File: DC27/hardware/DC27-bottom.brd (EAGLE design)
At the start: 102.4 x 117.6 mm, 86 parts, among them IC2 LDL112D33R, IC3 FT2232HL-REEL, IC4 93LC46BT-I_OT, J1 DN PAIR, J2 JTAG, J3 Battery, U2 ESP-WROOM-32, Y1 ABM7-12.000MHZ-D2Y-T

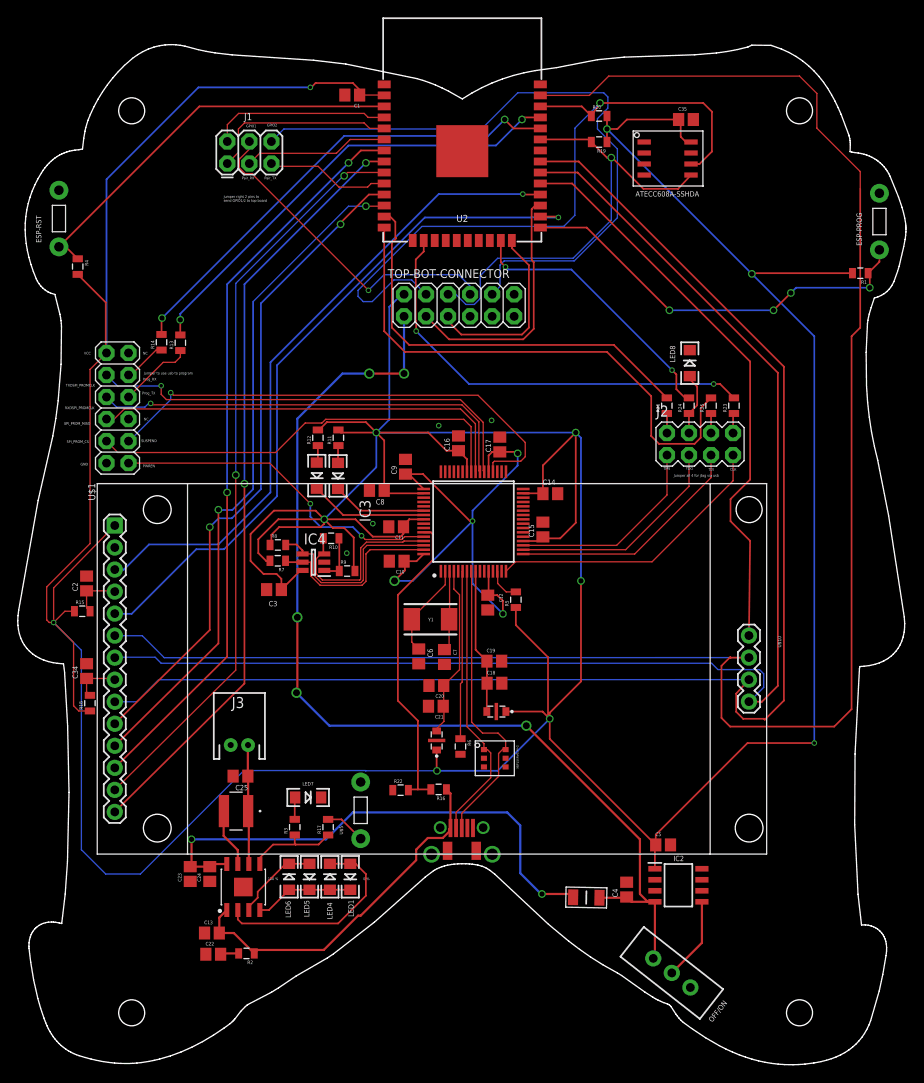
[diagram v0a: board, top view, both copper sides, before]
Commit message: Fixed copper ground planes
Fixed copper ground planes
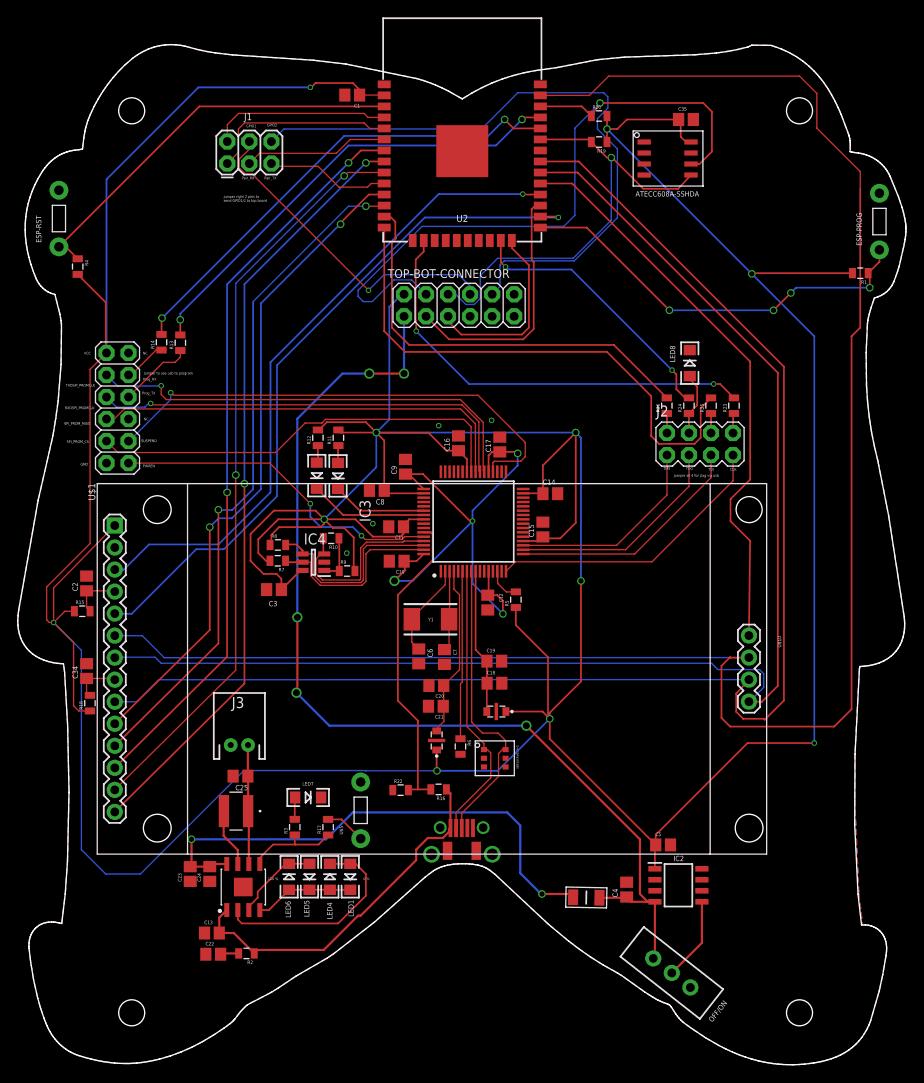
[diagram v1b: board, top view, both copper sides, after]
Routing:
- added copper zone on layer 1, net GND
- added copper zone on layer 16, net GND

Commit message: removed apa 102s from top board swapped led driver for atmega4089 put on programming pads bottom board adding paring headers on bottom board added 1206 56 OHM resistors to each LED top board pulled out UPDI pin on top board for programming the atmega chip
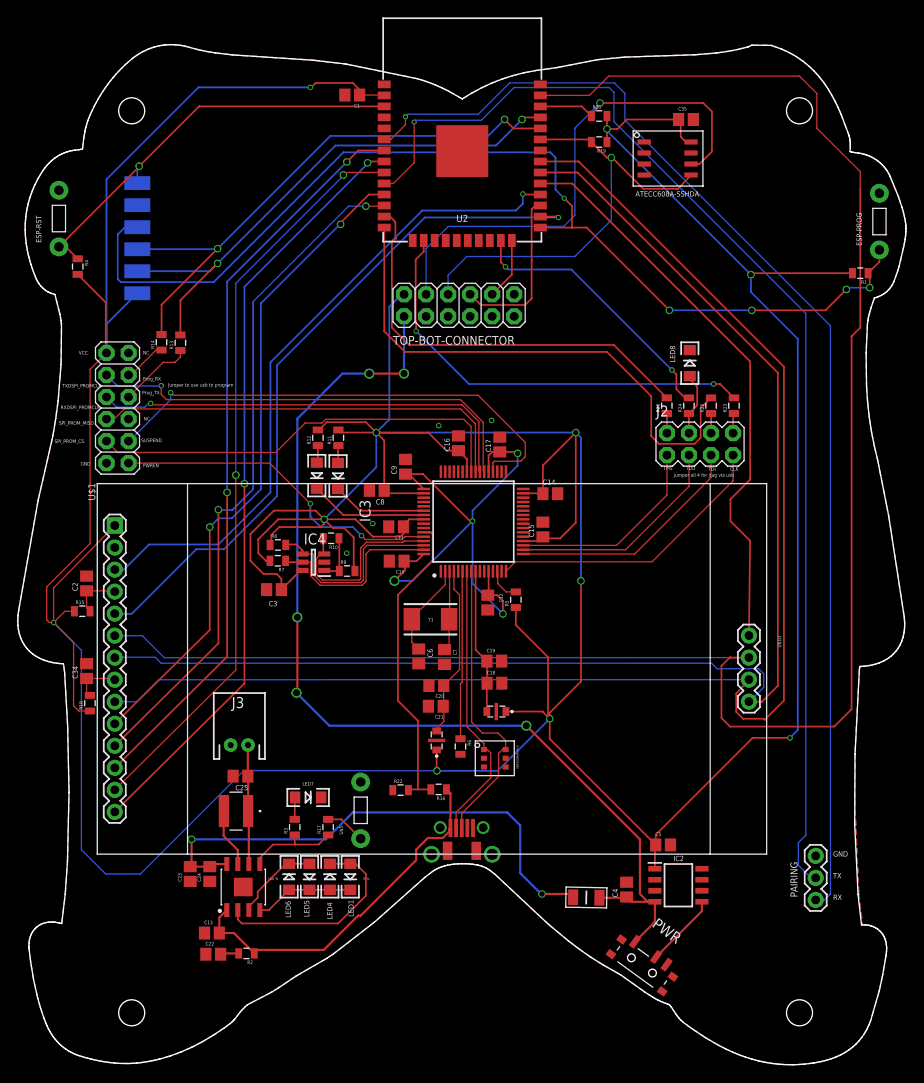
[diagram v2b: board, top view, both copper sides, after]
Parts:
- removed J1: DN PAIR, connector:2X3
- removed OFF/ON: Brd Power, switches:SWITCH-SPDT_KIT
- added J4: Program Port, connector:1X06-SMD-POGO
- added PWR: MSS3-V-T_R, switches:MSS3VTR
- added U$6: PAIRING, connector:1X03
- R3: value 10 R -> 1 K
- moved U$9 3.20 mm to (53.6, 108.0)
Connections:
- removed net N$2: IC2.5, OFF/ON.2
- removed net SAO-GPIO1: J1.4, TOP-BOT-CONNECTOR.8
- removed net SAO-GPIO2: J1.6, TOP-BOT-CONNECTOR.10
- new net EN: IC2.5, PWR.B1
- net APA102_CLK: now also TOP-BOT-CONNECTOR.10; no longer TOP-BOT-CONNECTOR.5
- net APA102_DATA: now also TOP-BOT-CONNECTOR.8; no longer TOP-BOT-CONNECTOR.3
- net ESP-EN: now also J4.1
- net ESP-IO0: now also J4.3
- net GND: now also J4.2, PWR.C1, U$6.3; no longer OFF/ON.1
- net PAIR_RX: now also U$6.1; no longer J1.3
- net PAIR_TX: now also U$6.2; no longer J1.5
- net PROG_RX: now also J4.4
- net PROG_TX: now also J4.5
- net SVN: no longer J1.1
- net SVP: no longer J1.2
- net VBAT: now also PWR.A1; no longer OFF/ON.3
- net VCC: now also J4.6
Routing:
- net PAIR_TX: track 14.3 -> 135.3 mm, vias 0 -> 1
- net PAIR_RX: track 16.7 -> 135.6 mm, vias 0 -> 1
- net SAO-GPIO2: track 76.2 -> 0.00 mm
- net ESP-IO0: track 48.0 -> 121.7 mm, vias 4 -> 5
- net SAO-GPIO1: track 38.2 -> 0.00 mm, vias 1 -> 0
- net SVN: track 21.9 -> 0.00 mm
- net SVP: track 20.8 -> 0.00 mm
- net SCL: track 82.3 -> 67.2 mm
- net APA102_CLK: track 21.7 -> 7.15 mm
- net PROG_TX: track 53.3 -> 63.9 mm
- net PROG_RX: track 55.4 -> 65.7 mm
- net APA102_DATA: track 29.1 -> 19.4 mm
- net N$2: track 9.64 -> 0.00 mm
- net EN: track 0.00 -> 8.55 mm
- net VCC: track 615.9 -> 620.8 mm
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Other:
- board text added: "PAIRING"
- board text added: "RX"
- board text added: "TX"
- board text removed: "GPIO1"
- board text removed: "GPIO2"
- board text removed: "Pair_RX"
- board text removed: "Pair_TX"
- board text removed: "jumper right 2 pins to send GPIO1/2 to top board"

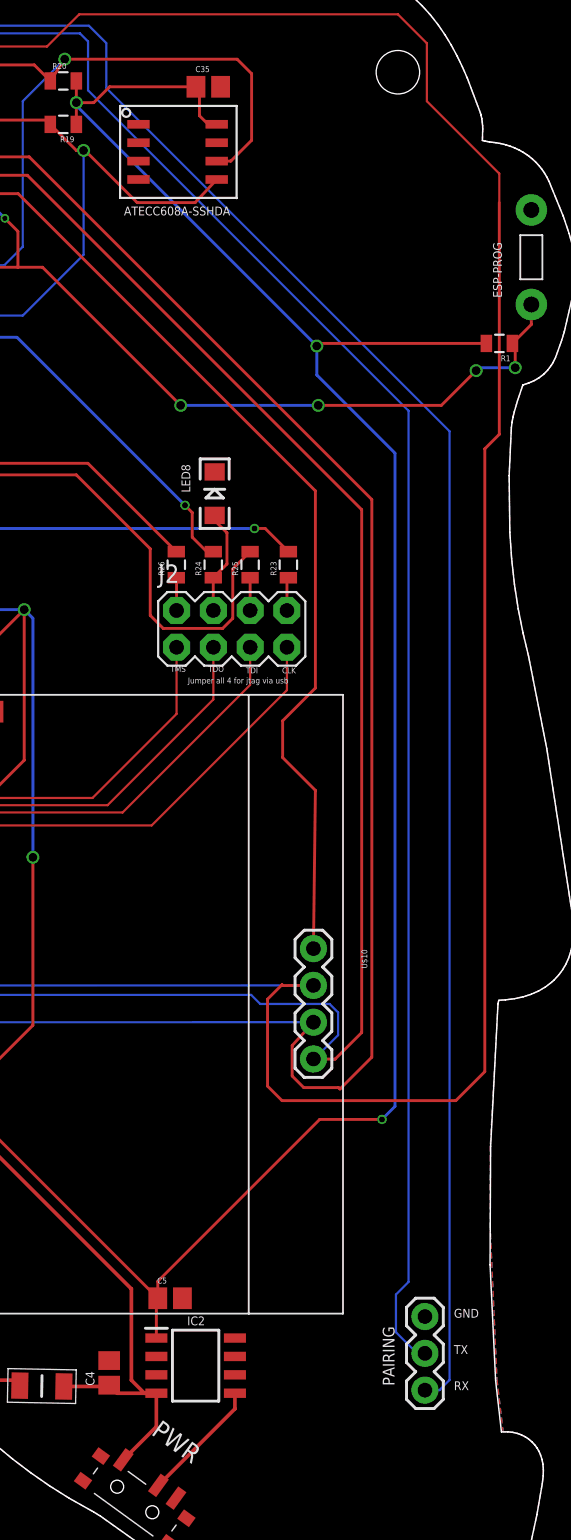
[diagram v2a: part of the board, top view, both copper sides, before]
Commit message: moved pairing headers back so they don't stick out
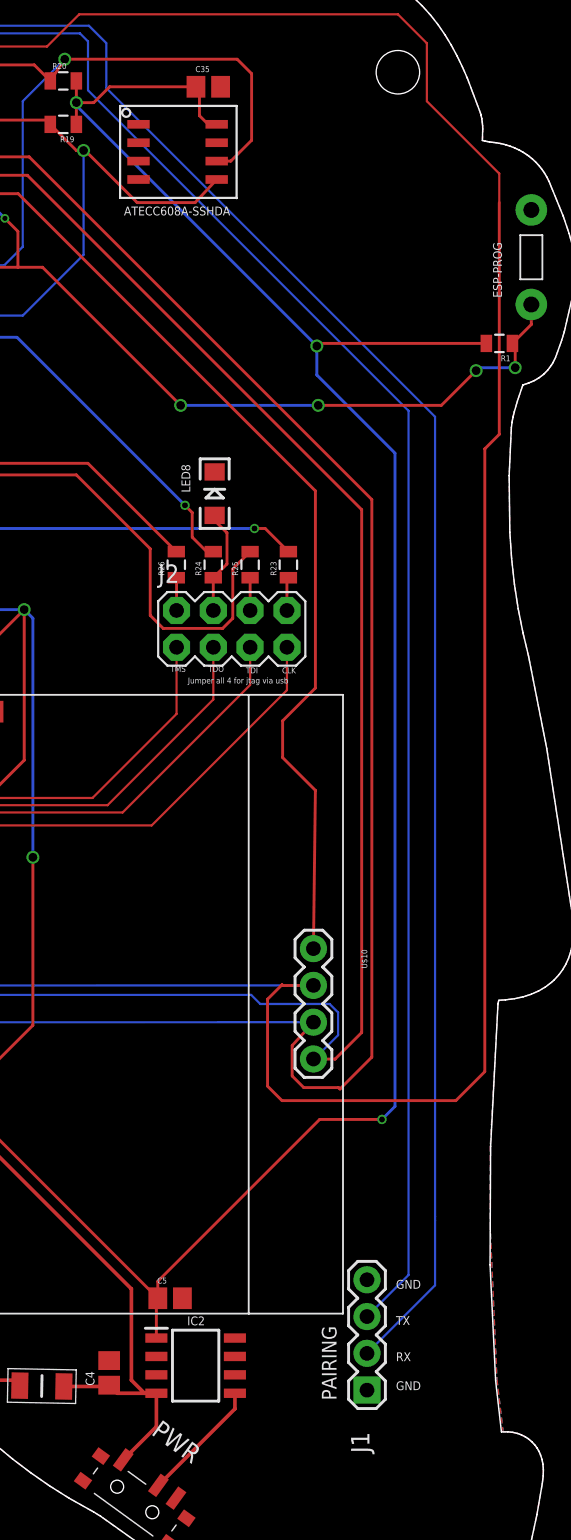
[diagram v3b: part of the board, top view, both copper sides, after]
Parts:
- removed U$6: PAIRING, connector:1X03
- added J1: PAIRING, connector:1X04
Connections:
- net GND: now also J1.1, J1.4; no longer U$6.3
- net PAIR_RX: now also J1.2; no longer U$6.1
- net PAIR_TX: now also J1.3; no longer U$6.2
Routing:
- net PAIR_TX: track 135.3 -> 132.4 mm
- net PAIR_RX: track 135.6 -> 133.3 mm
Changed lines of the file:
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@@
 <wire x1="102.410565625" y1="96.36026875" x2="102.405075" y2="96.583146875" width="0.1" layer="20"/>
 <wire x1="102.39045625" y1="96.807034375" x2="102.405075" y2="96.583146875" width="0.1" layer="20"/>
-<text x="94" y="19" size="0.6096" layer="25">RX</text>
-<text x="94" y="21.5" size="0.6096" layer="25">TX</text>
-<text x="94" y="24" size="0.6096" layer="25">GND</text>
-<text x="89.9" y="19.3" size="0.8128" layer="25" font="vector" rot="R90">PAIRING</text>
+<text x="90" y="21" size="0.6096" layer="25" font="vector">RX</text>
+<text x="90" y="23.5" size="0.6096" layer="25" font="vector">TX</text>
+<text x="90" y="26" size="0.6096" layer="25" font="vector">GND</text>
+<text x="85.9" y="18.3" size="1.016" layer="25" font="vector" rot="R90">PAIRING</text>
+<text x="90" y="19" size="0.6096" layer="25" font="vector">GND</text>
 </plain>
 <attributes>
@@
 <attribute name="NAME" x="43.244228125" y="83.014059375" size="1.016" layer="25" ratio="10"/>
 </element>
-<element name="U$6" library="connector" package="1X03" value="PAIRING" x="92" y="19" smashed="yes" rot="R90">
-<attribute name="VALUE" x="95.175" y="17.73" size="1.27" layer="27" rot="R90"/>
-</element>
 <element name="PWR" library="switches" package="MSS3VTR" value="MSS3-V-T_R" x="71.2" y="10.4" smashed="yes" rot="R324">
 <attribute name="DESCRIPTION" value="Slide Switches Slide Type 1P2T (1.4mm height)" x="71.2" y="10.4" size="0.6096" layer="27" rot="R324" display="off"/>
@@
 <attribute name="NAME" x="11.16" y="96.57" size="0.8128" layer="26" rot="MR270"/>
 <attribute name="VALUE" x="16.875" y="97.205" size="0.8128" layer="28" rot="MR270"/>
+</element>
+<element name="J1" library="connector" package="1X04" value="PAIRING" x="88" y="19" smashed="yes" rot="R90">
+<attribute name="NAME" x="88.1712" y="14.6538" size="1.27" layer="25" ratio="10" rot="R90"/>
+<attribute name="PROD_ID" value="CONN-09696" x="88" y="19" size="1.778" layer="27" rot="R90" display="off"/>
+<attribute name="VALUE" x="91.175" y="17.73" size="1.27" layer="27" rot="R90"/>
 </element>
 </elements>
@@
 <vertex x="50.95815" y="111.519684375"/>
 </polygon>
-<contactref element="U$6" pad="3"/>
 <contactref element="PWR" pad="C1"/>
 <contactref element="J4" pad="2"/>
+<contactref element="J1" pad="4"/>
+<contactref element="J1" pad="1"/>
 </signal>
 <signal name="VCC">
@@
 <signal name="PAIR_RX">
 <contactref element="U2" pad="6"/>
-<contactref element="U$6" pad="1"/>
 <wire x1="53.1" y1="109.6" x2="56.7" y2="113.2" width="0.1524" layer="16"/>
 <wire x1="56.7" y1="113.2" x2="68.8" y2="113.2" width="0.1524" layer="16"/>
@@
 <wire x1="44.7" y1="109.3" x2="45" y2="109.6" width="0.1524" layer="16"/>
 <wire x1="53.1" y1="109.6" x2="45" y2="109.6" width="0.1524" layer="16"/>
-<wire x1="93.7" y1="85.2" x2="93.7" y2="19.7" width="0.1524" layer="16"/>
-<wire x1="93.7" y1="85.2" x2="70" y2="108.9" width="0.1524" layer="16"/>
-<wire x1="93.7" y1="19.7" x2="93" y2="19" width="0.1524" layer="16"/>
-<wire x1="93" y1="19" x2="92" y2="19" width="0.1524" layer="16"/>
+<wire x1="92.7" y1="86.2" x2="92.7" y2="31" width="0.1524" layer="16"/>
+<wire x1="92.7" y1="31" x2="92.7" y2="30.7" width="0.1524" layer="16"/>
+<wire x1="92.7" y1="86.2" x2="70" y2="108.9" width="0.1524" layer="16"/>
 <via x="44.7" y="109.3" extent="1-16" drill="0.35"/>
 <wire x1="42.250228125" y1="106.685059375" x2="42.258825" y2="106.6764625" width="0.1524" layer="1"/>
@@
 <wire x1="44.7" y1="109.3" x2="44.7" y2="108.38155" width="0.1524" layer="1"/>
 <wire x1="44.7" y1="108.38155" x2="42.9949125" y2="106.6764625" width="0.1524" layer="1"/>
+<contactref element="J1" pad="2"/>
+<wire x1="88" y1="21.54" x2="92.7" y2="26.24" width="0.1524" layer="16"/>
+<wire x1="92.7" y1="26.24" x2="92.7" y2="30.7" width="0.1524" layer="16"/>
 </signal>
 <signal name="PAIR_TX">
 <contactref element="U2" pad="10"/>
-<contactref element="U$6" pad="2"/>
 <wire x1="57.226296875" y1="112.673703125" x2="68.180640625" y2="112.673703125" width="0.1524" layer="16"/>
 <wire x1="68.180640625" y1="112.673703125" x2="68.739028125" y2="112.115315625" width="0.1524" layer="16"/>
-<wire x1="68.739028125" y1="108.743946875" x2="90.8684" y2="86.614575" width="0.1524" layer="16"/>
+<wire x1="90.8684" y1="86.614575" x2="68.739028125" y2="108.743946875" width="0.1524" layer="16"/>
 <wire x1="68.739028125" y1="112.115315625" x2="68.739028125" y2="108.743946875" width="0.1524" layer="16"/>
 <wire x1="53.45259375" y1="108.9" x2="57.226296875" y2="112.673703125" width="0.1524" layer="16"/>
 <wire x1="53.45259375" y1="108.9" x2="45.9" y2="108.9" width="0.1524" layer="16"/>
 <wire x1="45.7" y1="108.7" x2="45.9" y2="108.9" width="0.1524" layer="16"/>
-<wire x1="90.8684" y1="86.614575" x2="90.8684" y2="26.4684" width="0.1524" layer="16"/>
-<wire x1="90" y1="25.6" x2="90" y2="23" width="0.1524" layer="16"/>
-<wire x1="90" y1="23" x2="91.46" y2="21.54" width="0.1524" layer="16"/>
-<wire x1="91.46" y1="21.54" x2="92" y2="21.54" width="0.1524" layer="16"/>
-<wire x1="90.8684" y1="26.4684" x2="90" y2="25.6" width="0.1524" layer="16"/>
 <wire x1="42.250228125" y1="101.605059375" x2="43.305059375" y2="101.605059375" width="0.1524" layer="1"/>
 <wire x1="45.7" y1="104" x2="45.7" y2="108.7" width="0.1524" layer="1"/>
 <via x="45.7" y="108.7" extent="1-16" drill="0.35"/>
 <wire x1="43.305059375" y1="101.605059375" x2="45.7" y2="104" width="0.1524" layer="1"/>
+<contactref element="J1" pad="3"/>
+<wire x1="88" y1="24.08" x2="90.8684" y2="26.9484" width="0.1524" layer="16"/>
+<wire x1="90.8684" y1="26.9484" x2="90.8684" y2="86.614575" width="0.1524" layer="16"/>
 </signal>
 <signal name="DISPLAY_RESET">
